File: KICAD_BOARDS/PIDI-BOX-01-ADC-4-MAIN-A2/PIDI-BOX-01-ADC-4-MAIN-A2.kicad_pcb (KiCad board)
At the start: 2 copper layers, 86 x 33 mm, 87 parts, among them IC1 HCPL-354-000E, J1 Conn_01x10_Pin, J10 Conn_01x01, J2 Conn_02x03_Odd_Even, J3 Conn_02x02_Odd_Even, J4 Conn_02x01, J5 Conn_02x01, J6 CTB0709_3, J7 CTB0709_3, J8 CTB0709_2, J9 Conn_01x01, Q1 BC808, U1 AMS1117-3.3, U2 ADuM1250, U3 AMS1117CD, U4 ADS1115IDGS

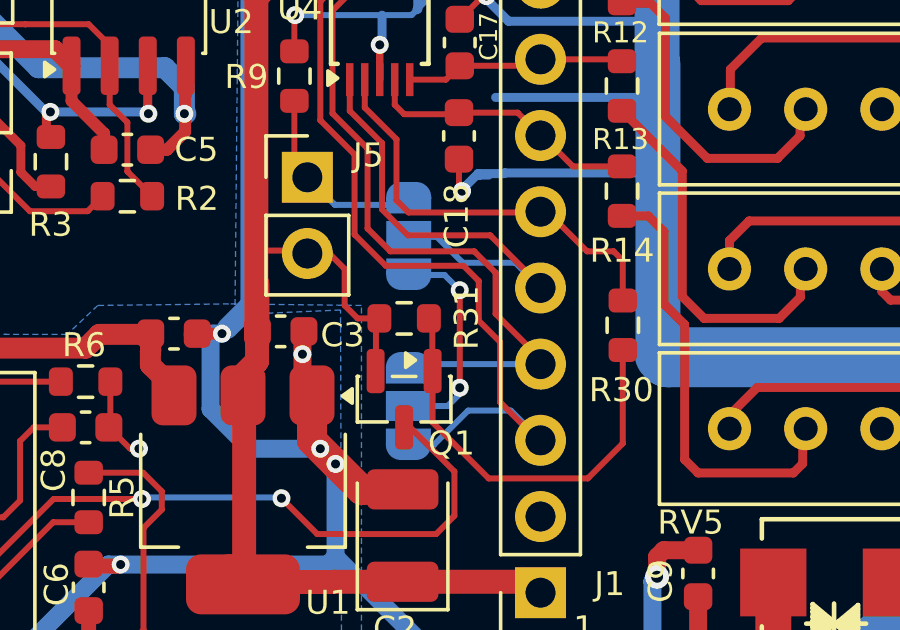
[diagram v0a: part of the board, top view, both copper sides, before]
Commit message: ADC4 change
ADC4 Update Solderjumper 1-2 closed now
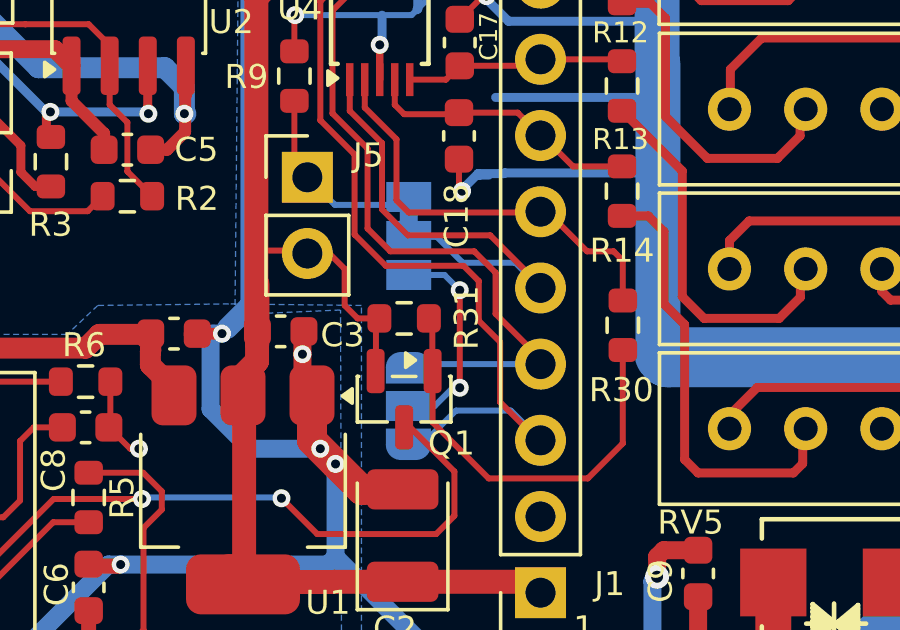
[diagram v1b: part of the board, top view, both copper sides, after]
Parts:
- JP4: footprint Jumper:SolderJumper-3_P1.3mm_Open_RoundedPad1.0x1.5mm -> Jumper:SolderJumper-3_P1.3mm_Bridged12_Pad1.0x1.5mm
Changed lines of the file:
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@@
 		(embedded_fonts no)
 	)
-	(footprint "Jumper:SolderJumper-3_P1.3mm_Open_RoundedPad1.0x1.5mm"
+	(footprint "Jumper:SolderJumper-3_P1.3mm_Bridged12_Pad1.0x1.5mm"
 		(layer "B.Cu")
 		(at 154.1272 73.3252 -90)
-		(descr "SMD Solder 3-pad Jumper, 1x1.5mm rounded Pads, 0.3mm gap, open")
-		(tags "solder jumper open")
+		(descr "SMD Solder 3-pad Jumper, 1x1.5mm Pads, 0.3mm gap, pads 1-2 bridged with 1 copper strip")
+		(tags "net tie solder jumper bridged")
 		(property "Reference" "JP4"
-			(at 0.0808 -2.1844 90)
+			(at 0 1.8 90)
 			(layer "B.SilkS")
 			(effects
 				(font
-					(size 0.8 0.8)
-					(thickness 0.1)
+					(size 1 1)
+					(thickness 0.15)
 				)
 				(justify mirror)
@@
 		)
 		(property "Value" "SolderJumper_3_Open"
-			(at 0 -1.9 90)
+			(at 0 -2 90)
 			(layer "B.Fab")
-			(hide yes)
 			(effects
 				(font
-					(size 0.8 0.8)
-					(thickness 0.1)
+					(size 1 1)
+					(thickness 0.15)
 				)
 				(justify mirror)
@@
 			)
 		)
-		(property "Description" "Solder Jumper, 3-pole, open"
+		(property "Description" "3-pole Solder Jumper, pins 1+2 closed/bridged"
 			(at 0 0 90)
 			(unlocked yes)
@@
 			)
 		)
-		(property ki_fp_filters "SolderJumper*Open*")
+		(property ki_fp_filters "SolderJumper*Bridged12*")
 		(sheetname "/")
 		(sheetfile "PIDI-BOX-01-ADC-4-MAIN-A2.kicad_sch")
 		(zone_connect 1)
 		(attr exclude_from_pos_files exclude_from_bom allow_soldermask_bridges)
+		(net_tie_pad_groups "1, 2")
+		(fp_poly
+			(pts
+				(xy -0.9 0.3) (xy -0.4 0.3) (xy -0.4 -0.3) (xy -0.9 -0.3)
+			)
+			(stroke
+				(width 0)
+				(type solid)
+			)
+			(fill yes)
+			(layer "B.Cu")
+		)
 		(fp_rect
-			(start -0.75 0.75)
-			(end 0.75 -0.75)
+			(start -0.8 0.75)
+			(end 0.8 -0.75)
 			(stroke
 				(width 0)
@@
 		)
 		(fp_line
-			(start -1.4 1)
-			(end 1.4 1)
+			(start -2.05 1)
+			(end 2.05 1)
 			(stroke
 				(width 0.12)
@@
 		)
 		(fp_line
-			(start 2.05 0.3)
-			(end 2.05 -0.3)
+			(start 2.05 1)
+			(end 2.05 -1)
 			(stroke
 				(width 0.12)
@@
 		)
 		(fp_line
-			(start -2.05 -0.3)
-			(end -2.05 0.3)
+			(start -2.05 -1)
+			(end -2.05 1)
 			(stroke
 				(width 0.12)
@@
 		)
 		(fp_line
-			(start 1.4 -1)
-			(end -1.4 -1)
+			(start 2.05 -1)
+			(end -2.05 -1)
 			(stroke
 				(width 0.12)
@@
 		)
 		(fp_line
-			(start -1.2 -1.2)
-			(end -1.5 -1.5)
+			(start -1.3 -1.2)
+			(end -1.6 -1.5)
 			(stroke
 				(width 0.12)
@@
 		)
 		(fp_line
-			(start -1.2 -1.2)
-			(end -0.9 -1.5)
+			(start -1.3 -1.2)
+			(end -1 -1.5)
 			(stroke
 				(width 0.12)
@@
 		)
 		(fp_line
-			(start -1.5 -1.5)
-			(end -0.9 -1.5)
-			(stroke
-				(width 0.12)
-				(type solid)
-			)
-			(layer "B.SilkS")
-		)
-		(fp_arc
-			(start -1.35 1)
-			(mid -1.844975 0.794975)
-			(end -2.05 0.3)
-			(stroke
-				(width 0.12)
-				(type solid)
-			)
-			(layer "B.SilkS")
-		)
-		(fp_arc
-			(start 2.05 0.3)
-			(mid 1.844975 0.794975)
-			(end 1.35 1)
-			(stroke
-				(width 0.12)
-				(type solid)
-			)
-			(layer "B.SilkS")
-		)
-		(fp_arc
-			(start -2.05 -0.3)
-			(mid -1.844975 -0.794975)
-			(end -1.35 -1)
-			(stroke
-				(width 0.12)
-				(type solid)
-			)
-			(layer "B.SilkS")
-		)
-		(fp_arc
-			(start 1.35 -1)
-			(mid 1.844975 -0.794975)
-			(end 2.05 -0.3)
+			(start -1.6 -1.5)
+			(end -1 -1.5)
 			(stroke
 				(width 0.12)
@@
 			(layer "B.CrtYd")
 		)
-		(pad "1" smd custom
+		(pad "1" smd rect
 			(at -1.3 0 270)
-			(size 1 0.5)
+			(size 1 1.5)
 			(layers "B.Cu" "B.Mask")
 			(net 56 "Net-(J5-Pin_1)")
 			(pinfunction "A")
 			(pintype "passive")
-			(zone_connect 2)
-			(thermal_bridge_angle 45)
-			(options
-				(clearance outline)
-				(anchor rect)
-			)
-			(primitives
-				(gr_circle
-					(center 0 -0.25)
-					(end 0.5 -0.25)
-					(width 0)
-					(fill yes)
-				)
-				(gr_circle
-					(center 0 0.25)
-					(end 0.5 0.25)
-					(width 0)
-					(fill yes)
-				)
-				(gr_poly
-					(pts
-						(xy 0.55 -0.75) (xy 0 -0.75) (xy 0 0.75) (xy 0.55 0.75)
-					)
-					(width 0)
-					(fill yes)
-				)
-			)
 		)
 		(pad "2" smd rect
@@
 			(pintype "passive")
 		)
-		(pad "3" smd custom
+		(pad "3" smd rect
 			(at 1.3 0 270)
-			(size 1 0.5)
+			(size 1 1.5)
 			(layers "B.Cu" "B.Mask")
 			(net 57 "Net-(JP3-C)")
 			(pinfunction "B")
 			(pintype "passive")
-			(zone_connect 2)
-			(thermal_bridge_angle 45)
-			(options
-				(clearance outline)
-				(anchor rect)
-			)
-			(primitives
-				(gr_circle
-					(center 0 -0.25)
-					(end 0.5 -0.25)
-					(width 0)
-					(fill yes)
-				)
-				(gr_circle
-					(center 0 0.25)
-					(end 0.5 0.25)
-					(width 0)
-					(fill yes)
-				)
-				(gr_poly
-					(pts
-						(xy 0 -0.75) (xy -0.55 -0.75) (xy -0.55 0.75) (xy 0 0.75)
-					)
-					(width 0)
-					(fill yes)
-				)
-			)
 		)
 		(embedded_fonts no)
@@
 	)
 	(segment
-		(start 156.1084 79.1464)
+		(start 155.702 79.1464)
 		(end 157.5308 79.1464)
 		(width 0.2)
@@
 	)
 	(segment
-		(start 158.517 80.137)
-		(end 158.275 79.895)
+		(start 154.5544 80.294)
+		(end 155.702 79.1464)
 		(width 0.2)
 		(layer "B.Cu")
@@
 	)
 	(segment
-		(start 154.1173 80.294)
-		(end 154.9608 80.294)
+		(start 158.517 80.137)
+		(end 158.275 79.895)
 		(width 0.2)
 		(layer "B.Cu")
@@
 	)
 	(segment
-		(start 154.9608 80.294)
-		(end 156.1084 79.1464)
+		(start 157.5308 79.1464)
+		(end 158.5214 80.137)
 		(width 0.2)
 		(layer "B.Cu")
@@
 	)
 	(segment
-		(start 157.5308 79.1464)
-		(end 158.5214 80.137)
+		(start 154.1173 80.294)
+		(end 154.5544 80.294)
 		(width 0.2)
 		(layer "B.Cu")
@@
 	)
 	(segment
-		(start 155.829 78.5876)
-		(end 155.4226 78.994)
+		(start 155.829 78.3844)
+		(end 155.6004 78.3844)
 		(width 0.2)
 		(layer "B.Cu")
@@
 	)
 	(segment
-		(start 155.4226 78.994)
-		(end 154.1173 78.994)
+		(start 155.321 74.6252)
+		(end 154.1272 74.6252)
 		(width 0.2)
 		(layer "B.Cu")
@@
 	)
 	(segment
-		(start 155.321 74.6252)
-		(end 154.1272 74.6252)
+		(start 155.829 75.1332)
+		(end 155.321 74.6252)
 		(width 0.2)
 		(layer "B.Cu")
@@
 	)
 	(segment
-		(start 155.829 75.1332)
-		(end 155.321 74.6252)
+		(start 155.6004 78.3844)
+		(end 154.9908 78.994)
 		(width 0.2)
 		(layer "B.Cu")
@@
 	)
 	(segment
-		(start 155.829 78.3844)
-		(end 155.829 78.5876)
+		(start 154.9908 78.994)
+		(end 154.1173 78.994)
 		(width 0.2)
 		(layer "B.Cu")
